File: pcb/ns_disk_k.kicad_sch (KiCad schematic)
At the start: 17 parts, among them J2 OLED Display, J3 Buttons, J4 MICRO-SD-CARD, P1 northstar card edge, U1 TXS0108EPW, U2 TXS0108EPW, U3 AMS1117-3.3

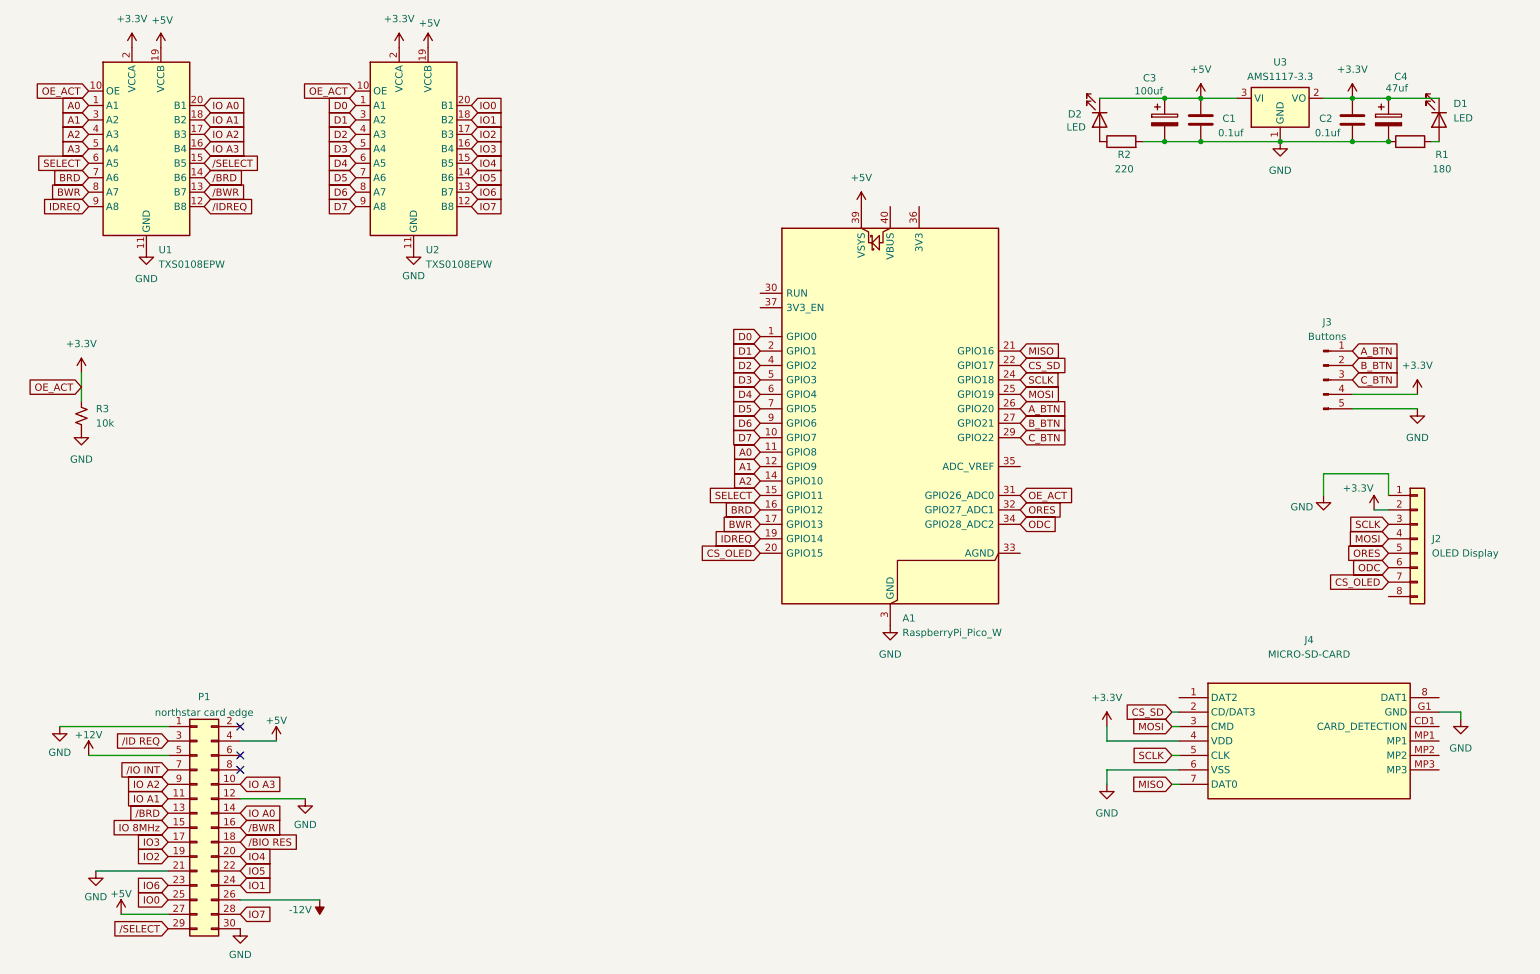
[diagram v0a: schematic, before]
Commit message: - Fix /ID REQ - Re-add /SELECT - A3 remains on level shifter no on pi-pico - Added header pins for power - Added holes to pcb
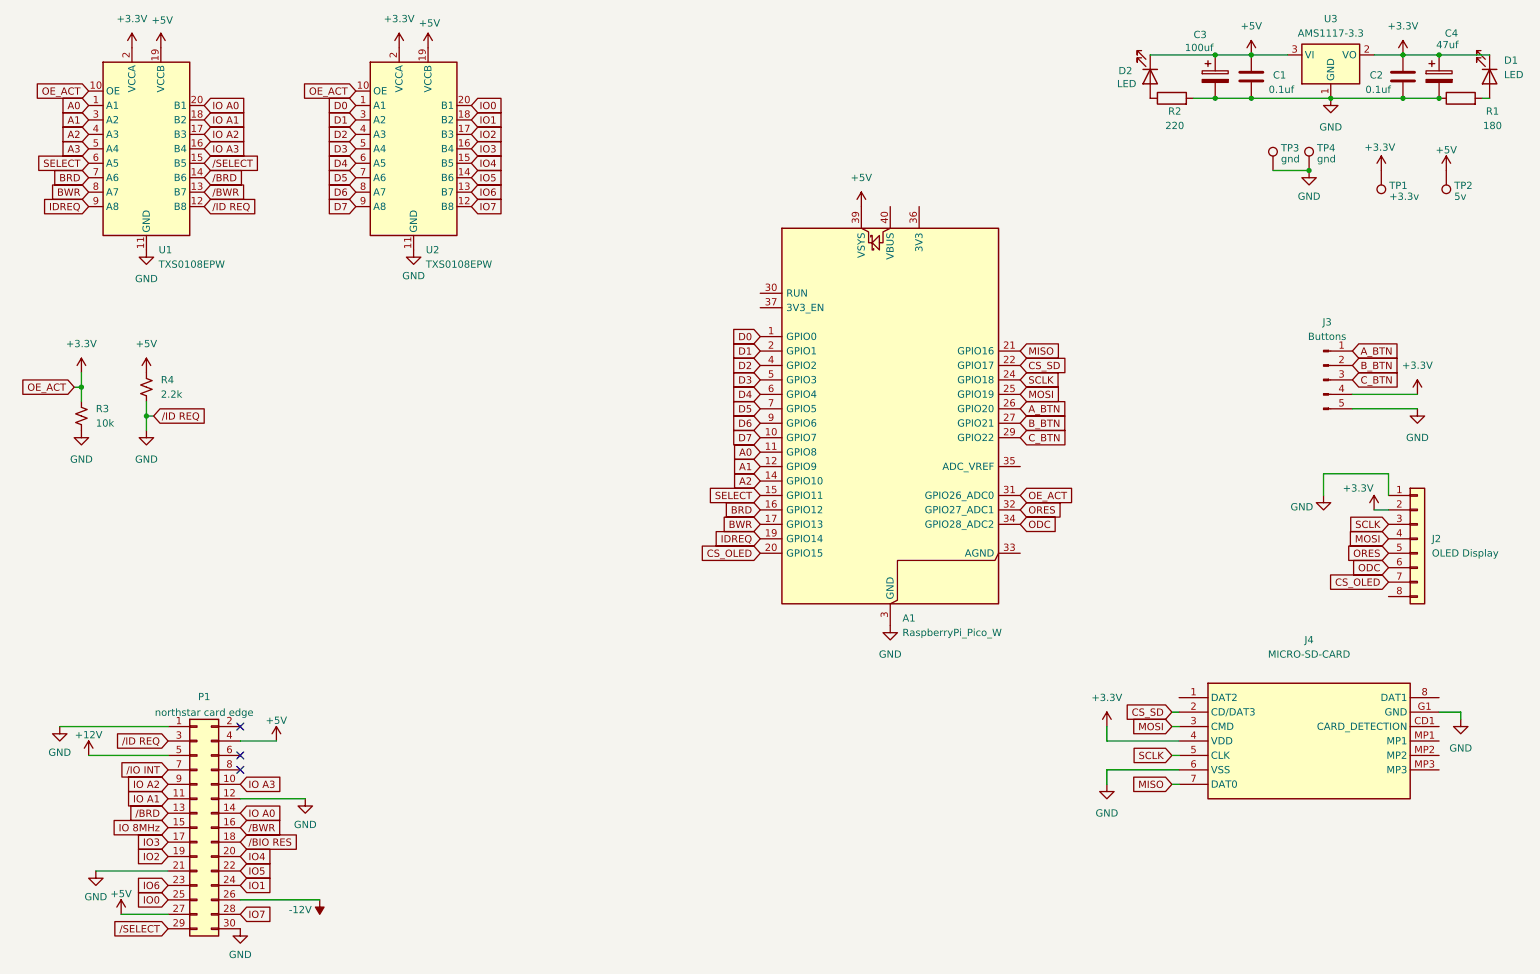
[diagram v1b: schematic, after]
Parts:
- added R4: 2.2k, Resistor_SMD:R_0603_1608Metric, symbol Device:R_Small_US
- added TP1: +3.3v, Connector_PinHeader_2.54mm:PinHeader_1x01_P2.54mm_Vertical, symbol Connector:TestPoint
- added TP2: 5v, Connector_PinHeader_2.54mm:PinHeader_1x01_P2.54mm_Vertical, symbol Connector:TestPoint
- added TP3, TP4: gnd, Connector_PinHeader_2.54mm:PinHeader_1x01_P2.54mm_Vertical, symbol Connector:TestPoint
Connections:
- net /IDREQ is gone; now on net GND: U1.12 (B8)
- net +3.3V: now also TP1.1
- net +5V: now also R4.1, TP2.1
- net GND: now also R4.2, TP3.1, TP4.1
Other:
- moved on the sheet: C1, C2, C3, C4, D1, D2, R1, R2, U3
